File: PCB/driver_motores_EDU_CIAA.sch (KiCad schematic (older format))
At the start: 37 parts

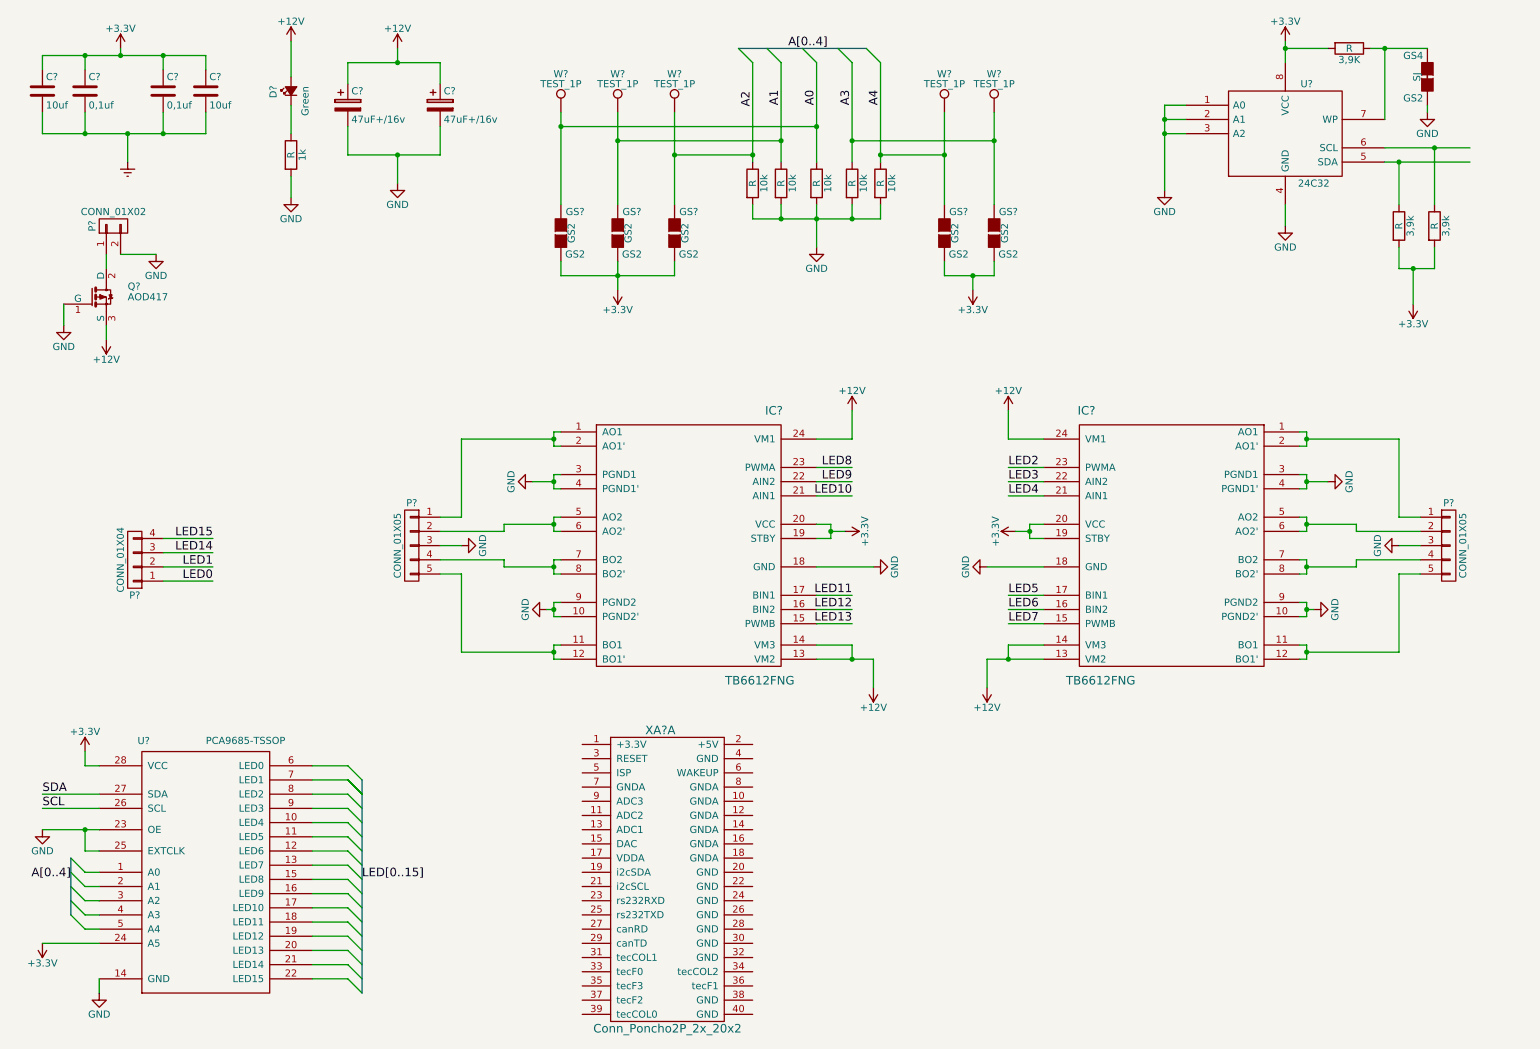
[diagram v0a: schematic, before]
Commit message: enumero los componentes, asocio los footprint, completo los valores de digikey
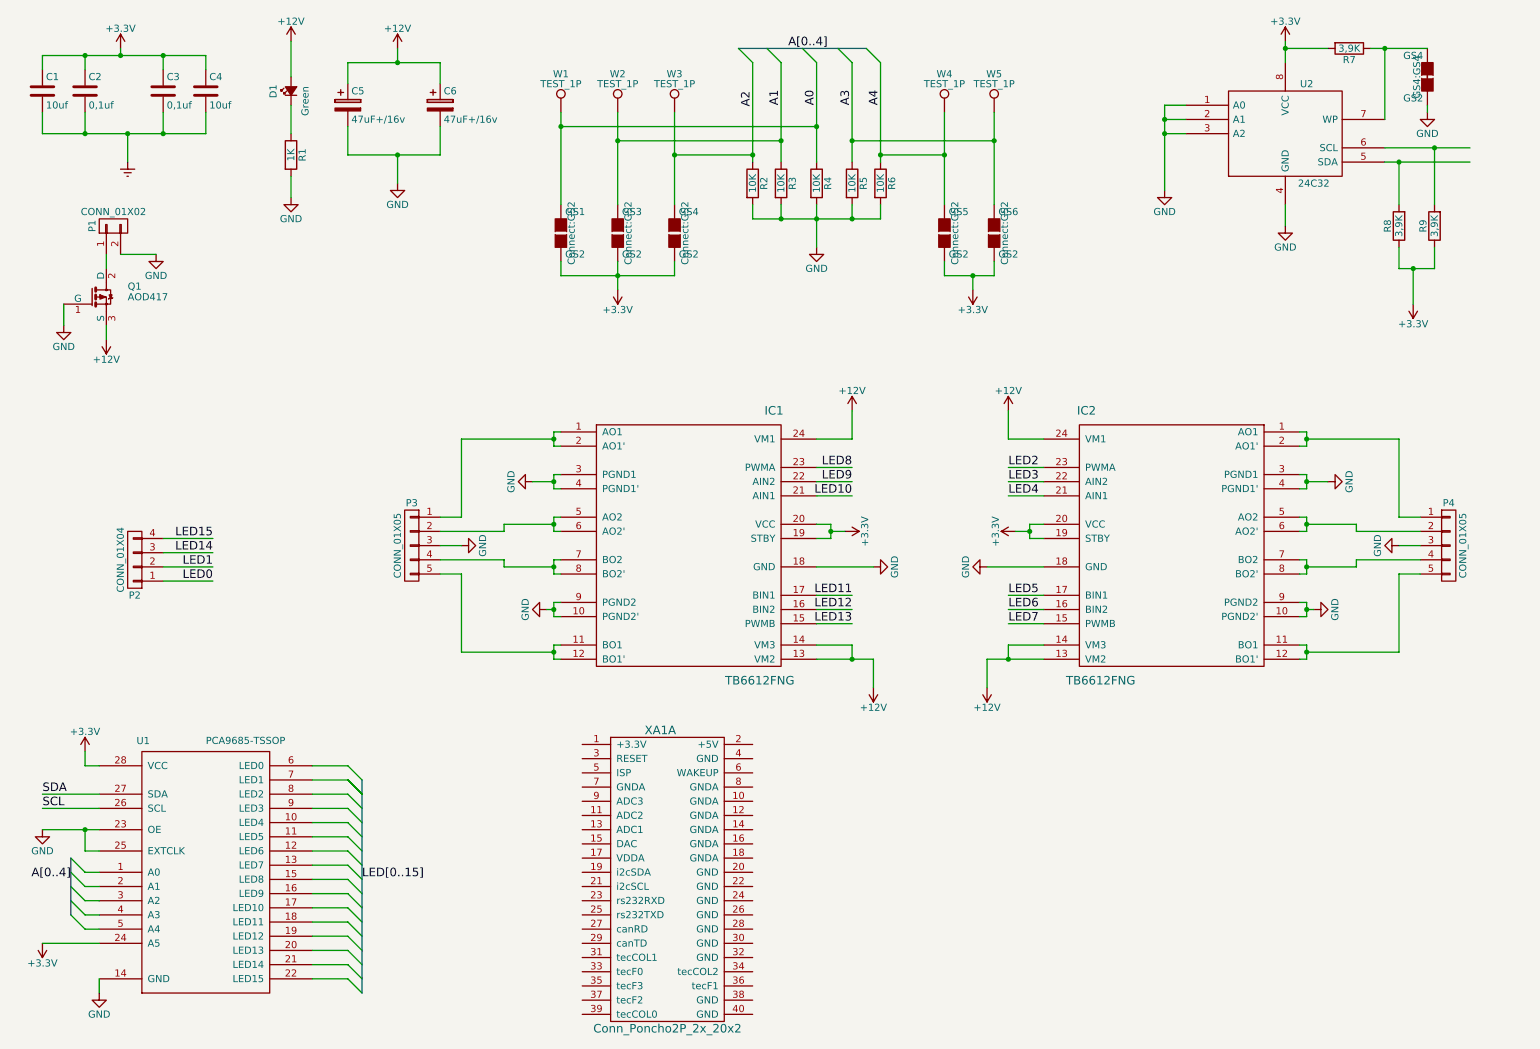
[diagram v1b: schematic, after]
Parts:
- removed 10k (x4), 3,9K, 3,9k (x2): R, symbol R
- added R3, R4, R5, R6: 10K, tp_final:R_1206_HandSoldering, symbol R
- added R7, R8, R9: 3,9K, tp_final:R_1206_HandSoldering, symbol R
- C1, C4: renamed from C?; footprint (none) -> tp_final:R_1206_HandSoldering; digikey# (none) -> 490-5961-2-ND
- C2, C3: renamed from C?; footprint (none) -> tp_final:R_1206_HandSoldering; digikey# (none) -> 311-1179-1-ND
- C5, C6: renamed from C?; footprint (none) -> tp_final:R_1206_HandSoldering; digikey# (none) -> 493-3095-2-ND
- D1: renamed from D?; footprint (none) -> tp_final:C_0603_HandSoldering; digikey# (none) -> 1516-1063-2-ND
- GS1, GS3, GS4, GS5, GS6: renamed from GS?; footprint GS2 -> Connect:GS2
- GS2: footprint SJ -> GS4:GS4
- IC1, IC2: renamed from IC?; footprint (none) -> w_smd_dil:ssop-24
- P1: renamed from P?; footprint (none) -> Sockets_MOLEX_KK-System:Socket_MOLEX-KK-RM2-54mm_Lock_2pin_straight; digikey# (none) -> 277-1721-ND
- P2: renamed from P?; footprint (none) -> Sockets_MOLEX_KK-System:Socket_MOLEX-KK-RM2-54mm_Lock_4pin_straight
- P3, P4: renamed from P?; footprint (none) -> Sockets_MOLEX_KK-System:Socket_MOLEX-KK-RM2-54mm_Lock_5pin_straight; digikey# (none) -> 277-1580-ND
- Q1: renamed from Q?; footprint (none) -> TO_SOT_Packages_SMD:TO-252-2Lead
- R1: renamed from 1k; value R -> 1K; footprint (none) -> tp_final:R_1206_HandSoldering; digikey# (none) -> RHM1.00KYTR-ND
- R2: renamed from 10k; value R -> 10K; footprint (none) -> tp_final:R_1206_HandSoldering; digikey# (none) -> RHM10KYTR-ND
- U1: renamed from U?; footprint MODULE -> w_smd_dil:tssop-28
- U2: renamed from U?; footprint (none) -> tp_final:SOIC-8; digikey# (none) -> CAT24C32WI-GT3TR-ND
- W1, W2, W3, W4, W5: renamed from W?; footprint (none) -> Measurement_Points:Test_Point
- XA1: renamed from XA?; footprint (none) -> tp_final:Conn_Poncho_Derecha
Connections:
- net +3V3: now also R7.2, R8.1, R9.1
- net A0: now also R4.1
- net A1: now also R3.1
- net A3: now also R5.1
- net A4: now also R6.1
- net GND: now also R3.2, R4.2, R5.2, R6.2
- net at U2.5 (SDA): now also R8.2
- net at U2.6 (SCL): now also R9.2
- net at GS2.2 (G2), U2.7 (WP): now also R7.1

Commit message: se corrigen errores de ERC, inicio de trabajo en pcb
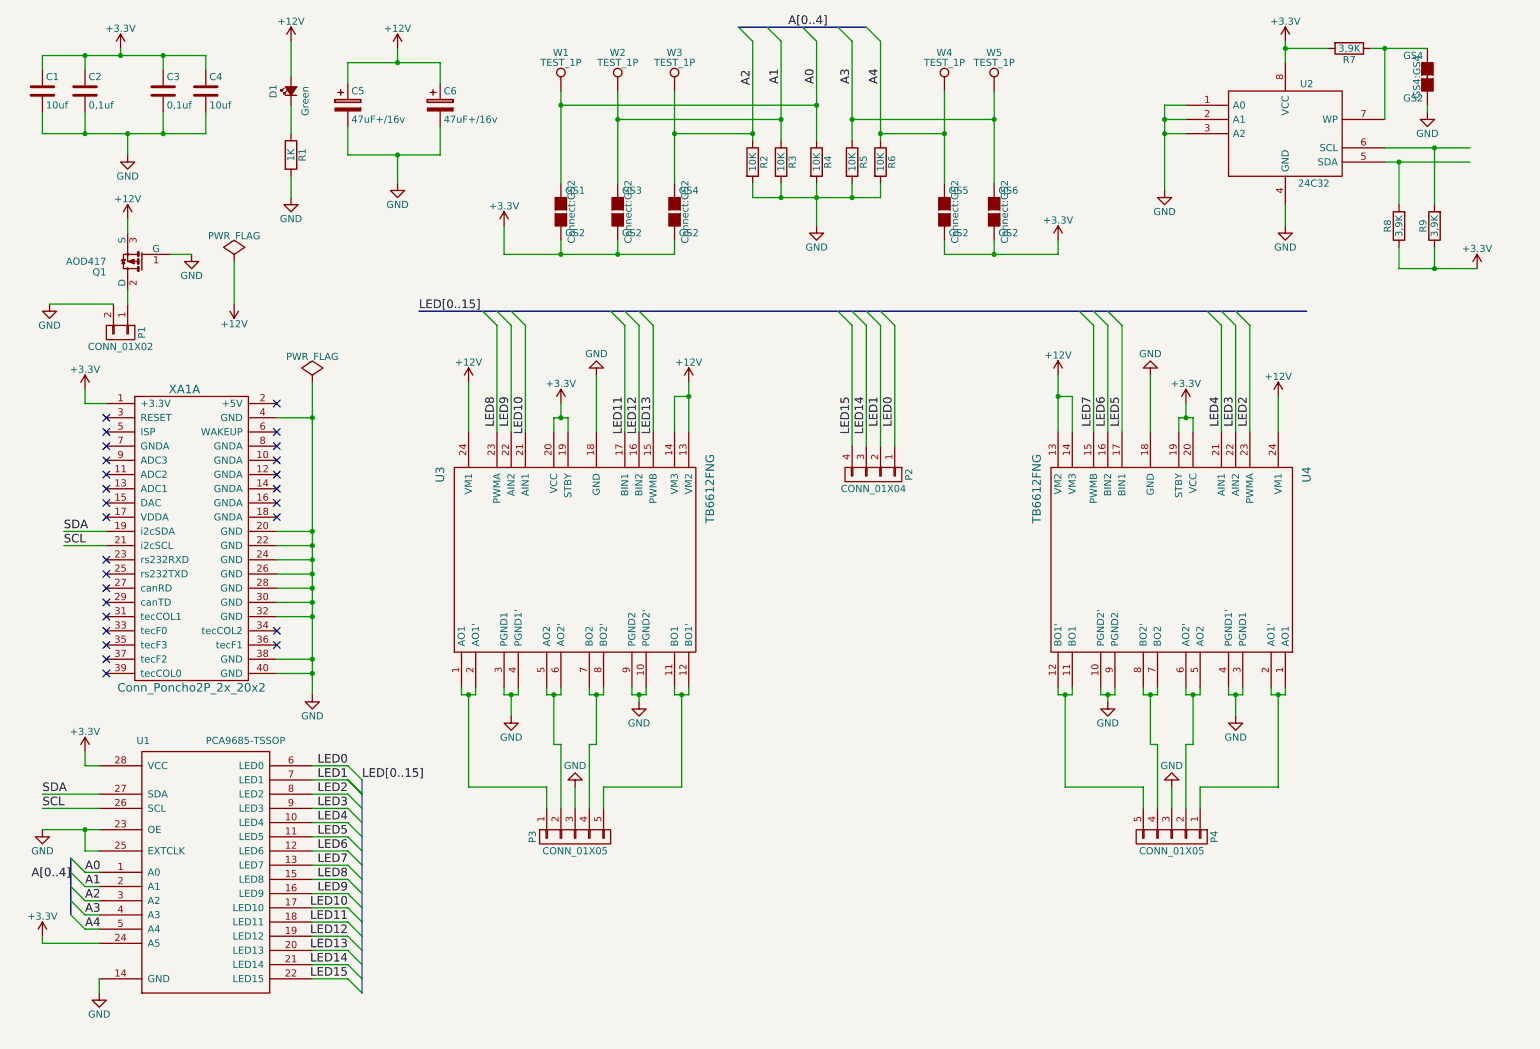
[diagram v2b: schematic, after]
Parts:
- renumbered IC1 to U3, IC2 to U4
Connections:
- net Earth is gone; now on net GND: C1.2, C2.2, C3.2, C4.2
- net +3V3: now also XA1.1 (+3.3V)
- net A0: now also U1.1 (A0)
- net A1: now also U1.2 (A1)
- net A2: now also U1.3 (A2)
- net A3: now also U1.4 (A3)
- net A4: now also U1.5 (A4)
- net GND: now also XA1.20 (GND), XA1.22 (GND), XA1.24 (GND), XA1.26 (GND), XA1.28 (GND), XA1.30 (GND), XA1.32 (GND), XA1.38 (GND), XA1.4 (GND), XA1.40 (GND)
- net LED0: now also U1.6 (LED0)
- net LED1: now also U1.7 (LED1)
- net LED10: now also U1.17 (LED10)
- net LED11: now also U1.18 (LED11)
- net LED12: now also U1.19 (LED12)
- net LED13: now also U1.20 (LED13)
- net LED14: now also U1.21 (LED14)
- net LED15: now also U1.22 (LED15)
- net LED2: now also U1.8 (LED2)
- net LED3: now also U1.9 (LED3)
- net LED4: now also U1.10 (LED4)
- net LED5: now also U1.11 (LED5)
- net LED6: now also U1.12 (LED6)
- net LED7: now also U1.13 (LED7)
- net LED8: now also U1.15 (LED8)
- net LED9: now also U1.16 (LED9)
- net SCL: now also XA1.21 (i2cSCL)
- net SDA: now also XA1.19 (i2cSDA)
- no-connect marks 0 -> 27
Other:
- moved on the sheet: GS1, GS3, GS4, GS5, GS6, P1, P2, P3, P4, Q1, R2, R3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

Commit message: termino ruteo, completo modulos 3D, modifico serigrafia
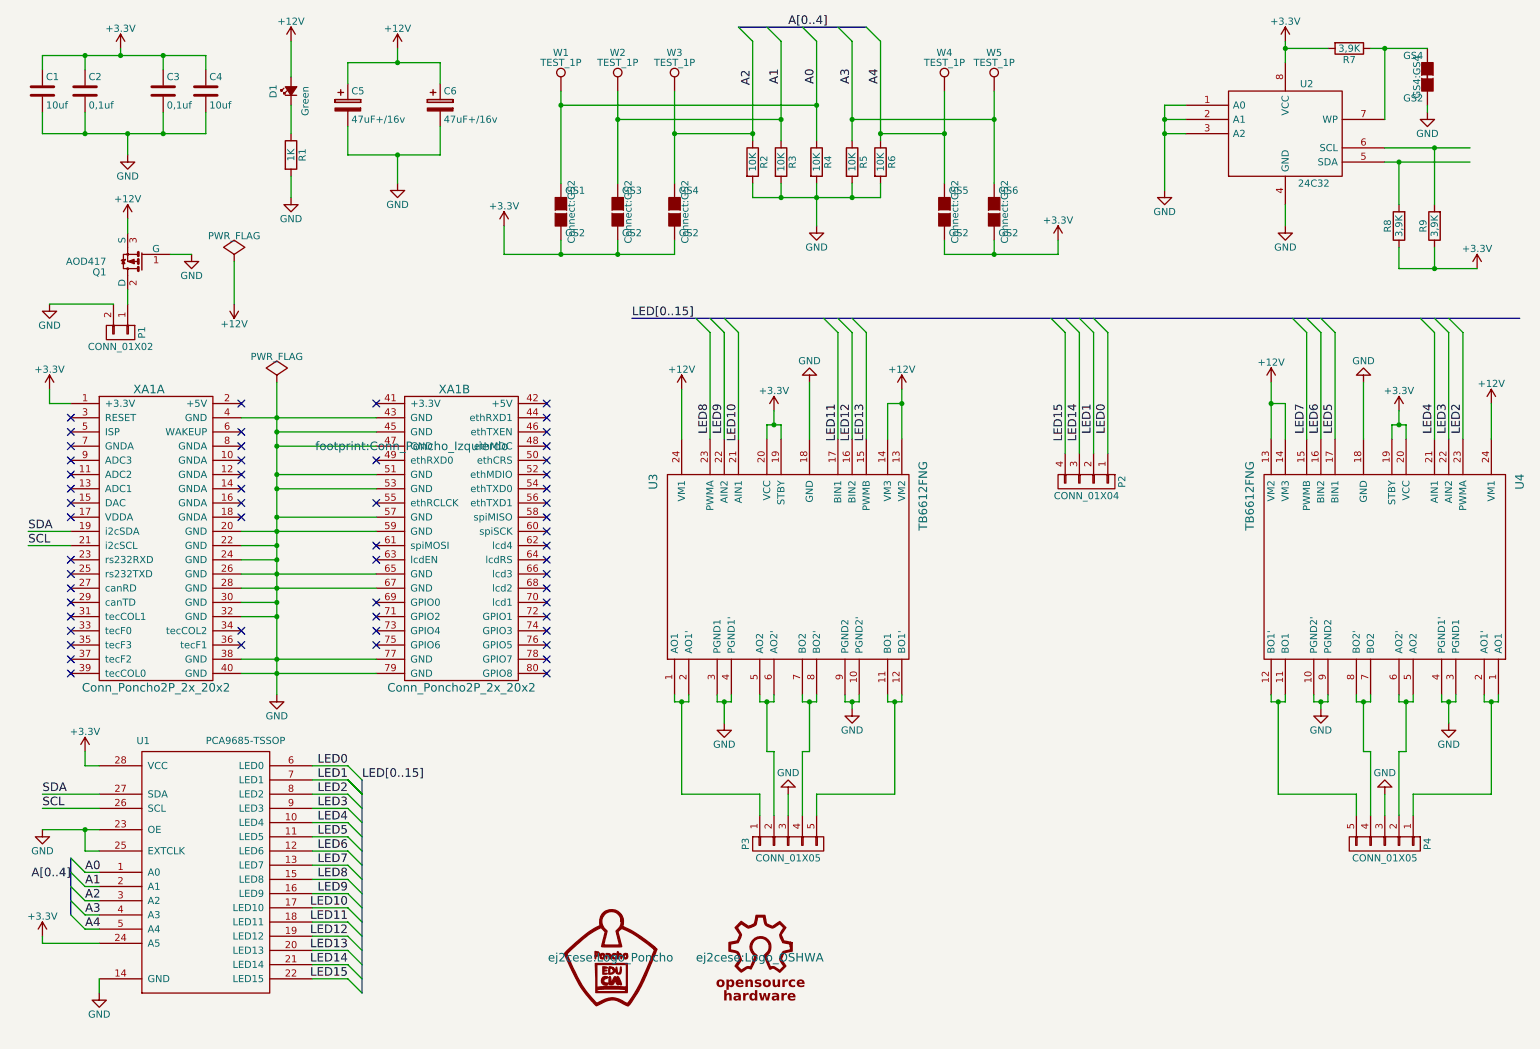
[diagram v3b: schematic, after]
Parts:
- added unit 2 of XA1
- C5, C6: footprint tp_final:R_1206_HandSoldering -> Capacitors_SMD:c_elec_5x5.3
- XA1: digikey# (none) -> 952-1387-ND
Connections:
- net GND: now also XA1.43 (GND), XA1.45 (GND), XA1.47 (GND), XA1.51 (GND), XA1.53 (GND), XA1.57 (GND), XA1.59 (GND), XA1.65 (GND), XA1.67 (GND), XA1.77 (GND), XA1.79 (GND)
- no-connect marks 27 -> 56
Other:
- moved on the sheet: P2, P3, P4, U3, U4, XA1A
